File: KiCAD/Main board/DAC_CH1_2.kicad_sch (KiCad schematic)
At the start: 73 parts, among them U1 LM4562, U1 PCM1789, U3 OPA1632DR, U4 OPA1632DR

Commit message: Ad good as finilized the main board schematic
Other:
- note added: "Adress=0"
- note added: "Combine I2C busses of the DACs? Otherwise they can get the same adress."
- note removed: "-Use Panasonic 0805 ERA series for audio path resistors -Use C0G MLCC capacitors for audio path capacitors"
- title: (none) -> AUDIO-DSP_MAIN_BOARD
- moved on the sheet: C1, C10, C11, C15, C16, C19, C2, C3, C4, C6, C7, C8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

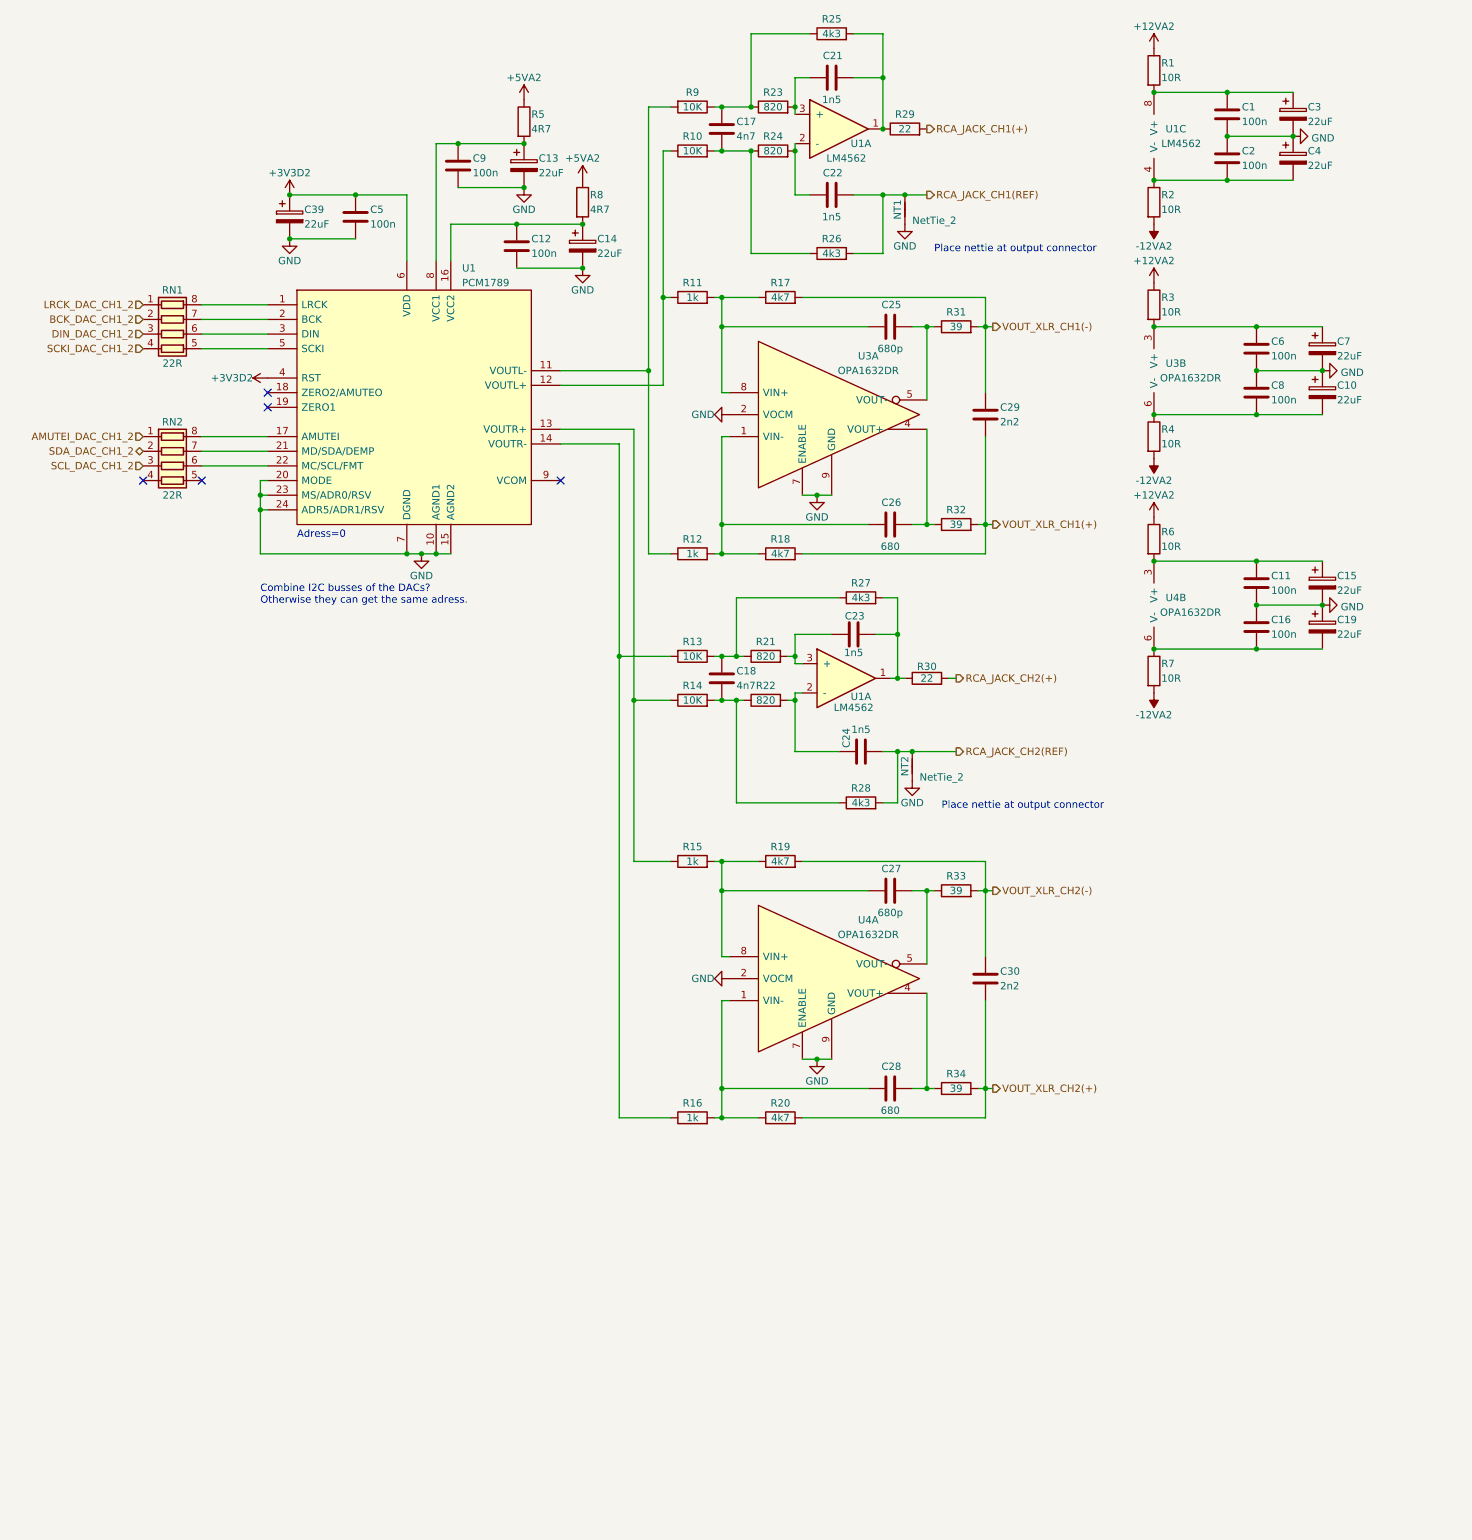
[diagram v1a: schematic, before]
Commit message: Finalizer main board schematic exept passive order links. Schematic ready for review
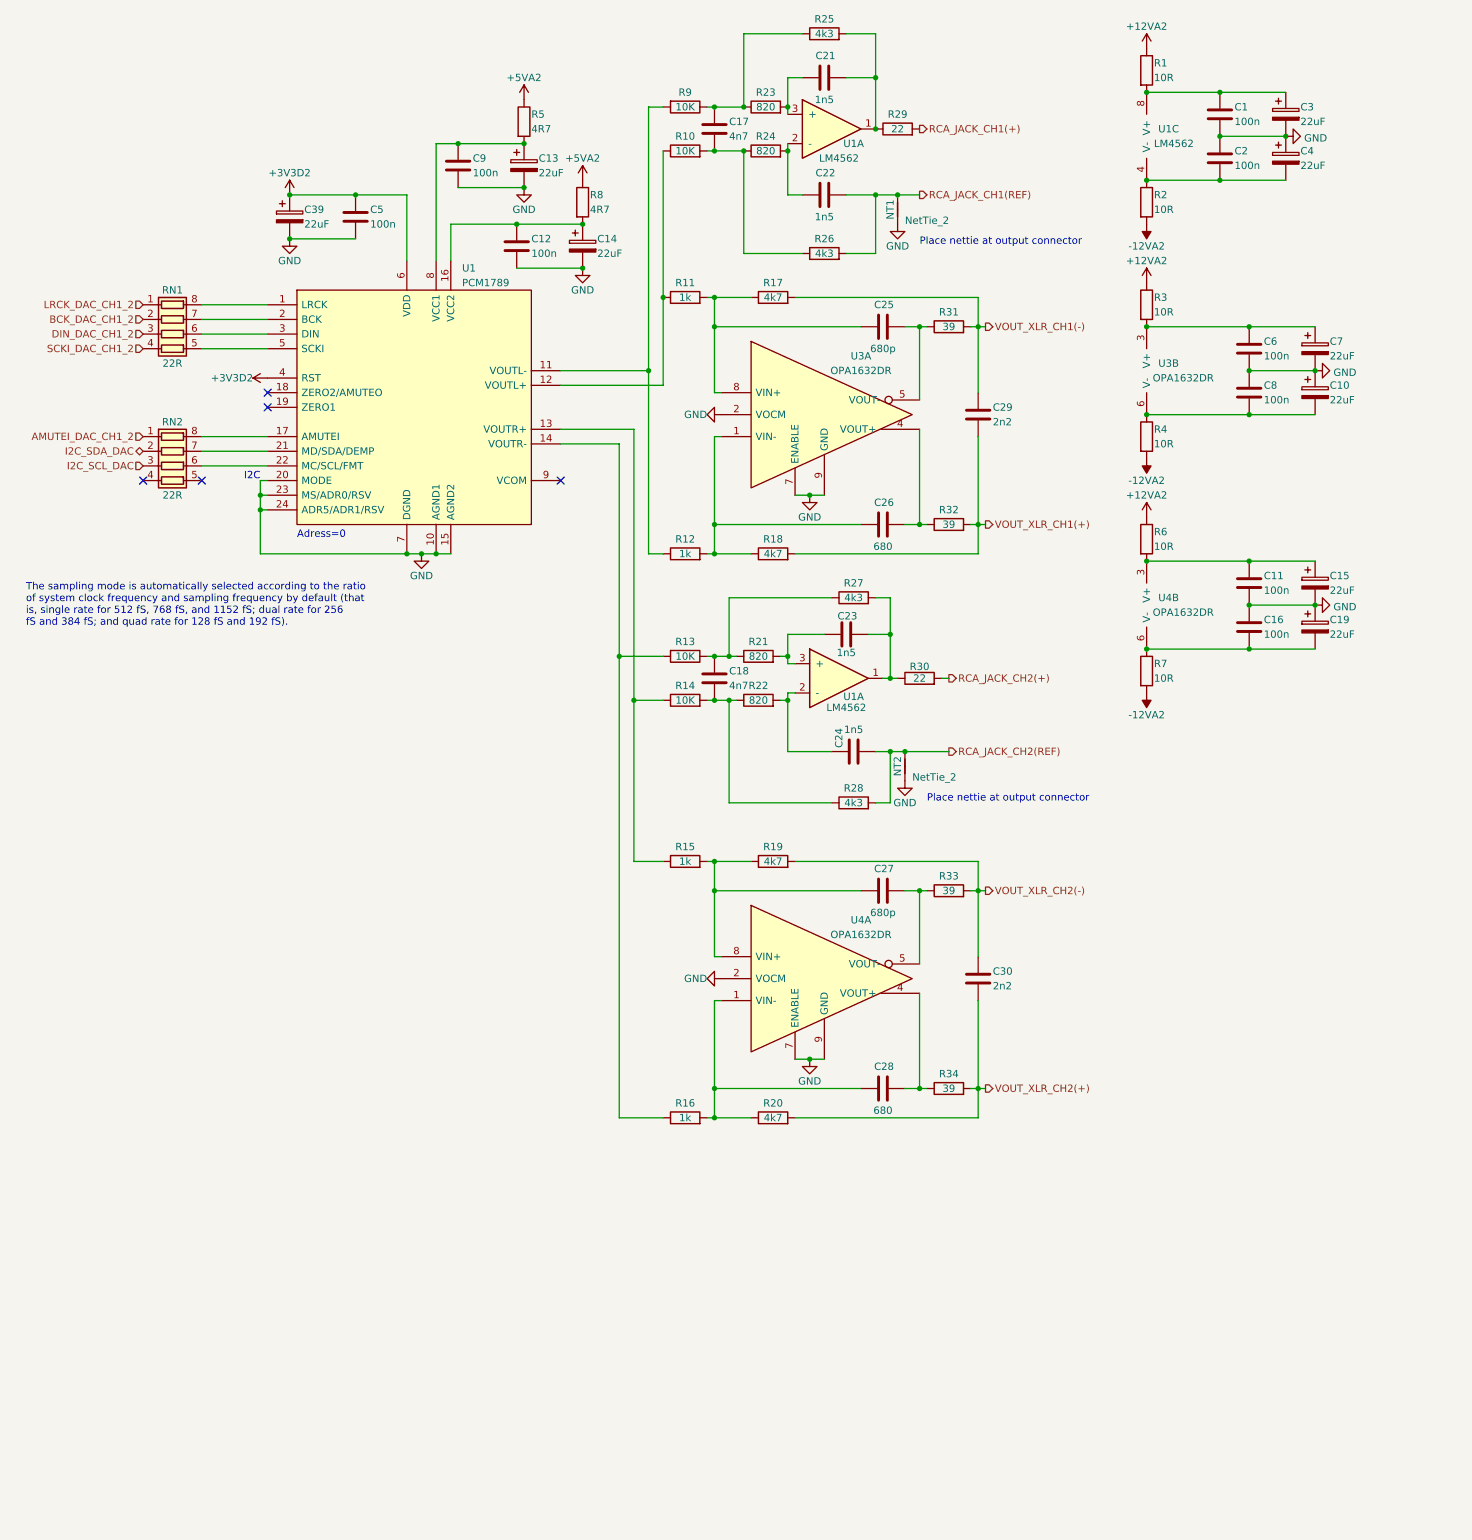
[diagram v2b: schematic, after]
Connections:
- net SCL_DAC_CH1_2 renamed I2C_SCL_DAC
- net SDA_DAC_CH1_2 renamed I2C_SDA_DAC
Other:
- note added: "I2C"
- note added: "The sampling mode is automatically selected according to the ratio of system clock frequency and sampling frequency by default (that is, single rate for 512 fS, 768 fS, and 1152 fS; dual rate for 256 fS and 384 fS; and quad rate for 128 fS and 192 fS)."
- note removed: "Combine I2C busses of the DACs? Otherwise they can get the same adress."
- moved on the sheet: C1, C10, C11, C15, C16, C17, C18, C19, C2, C21, C22, C23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

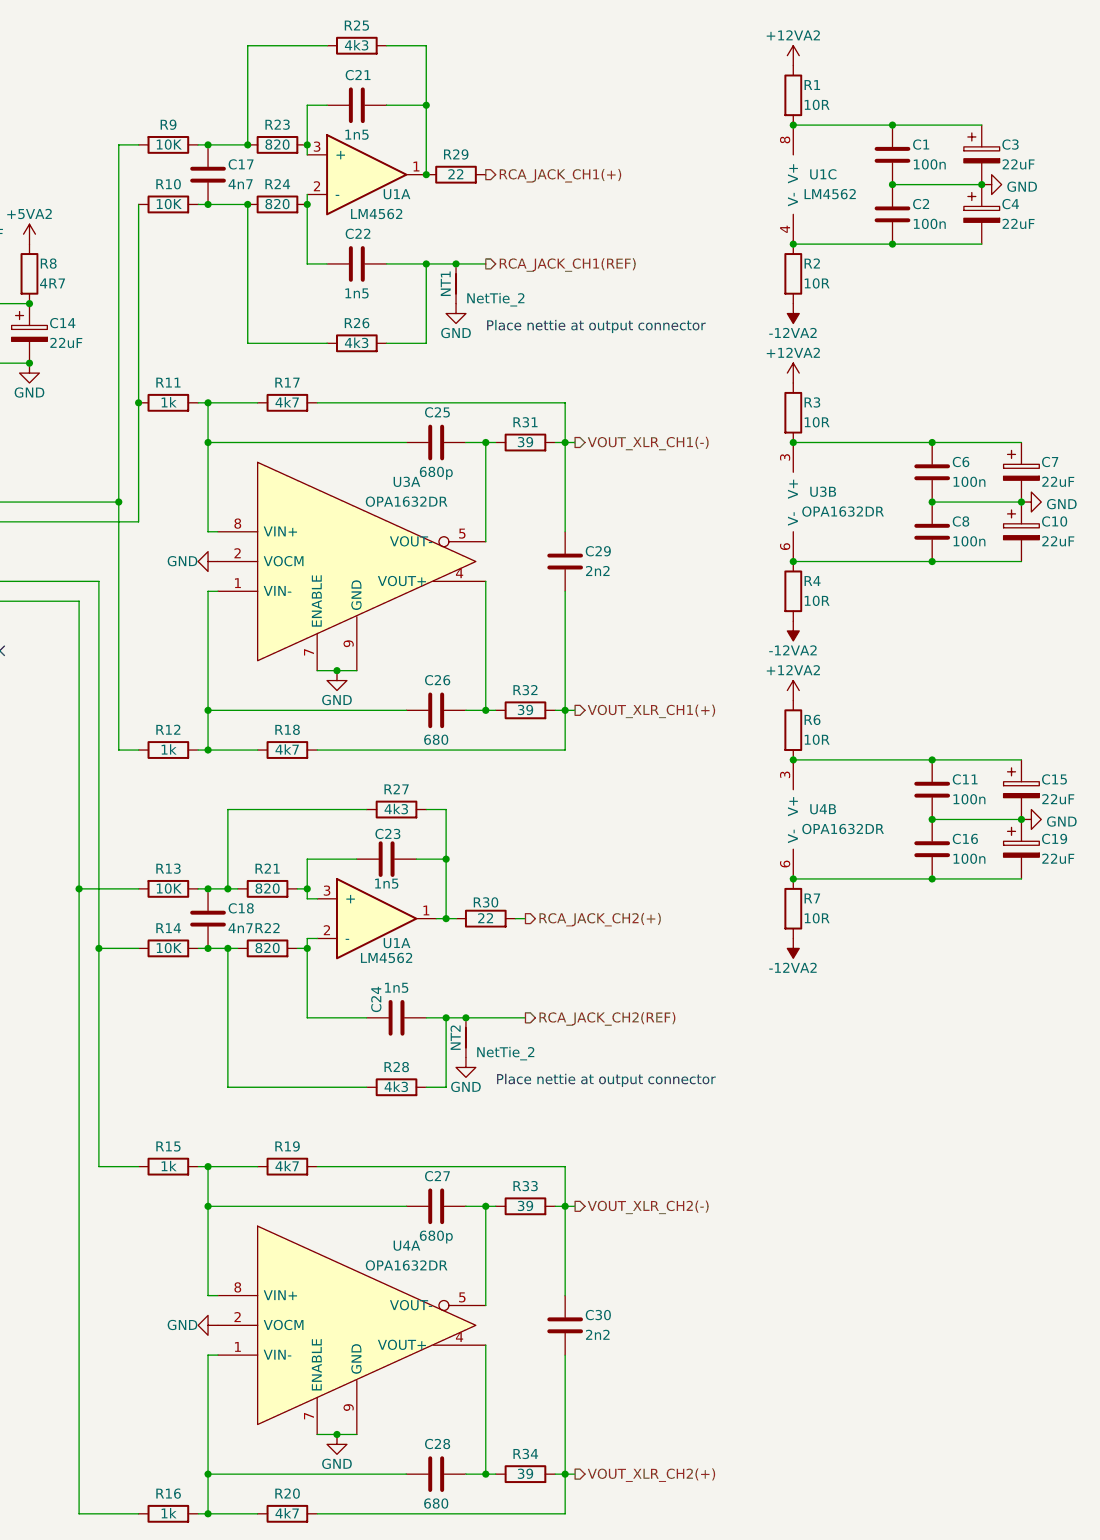
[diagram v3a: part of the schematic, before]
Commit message: Added component links
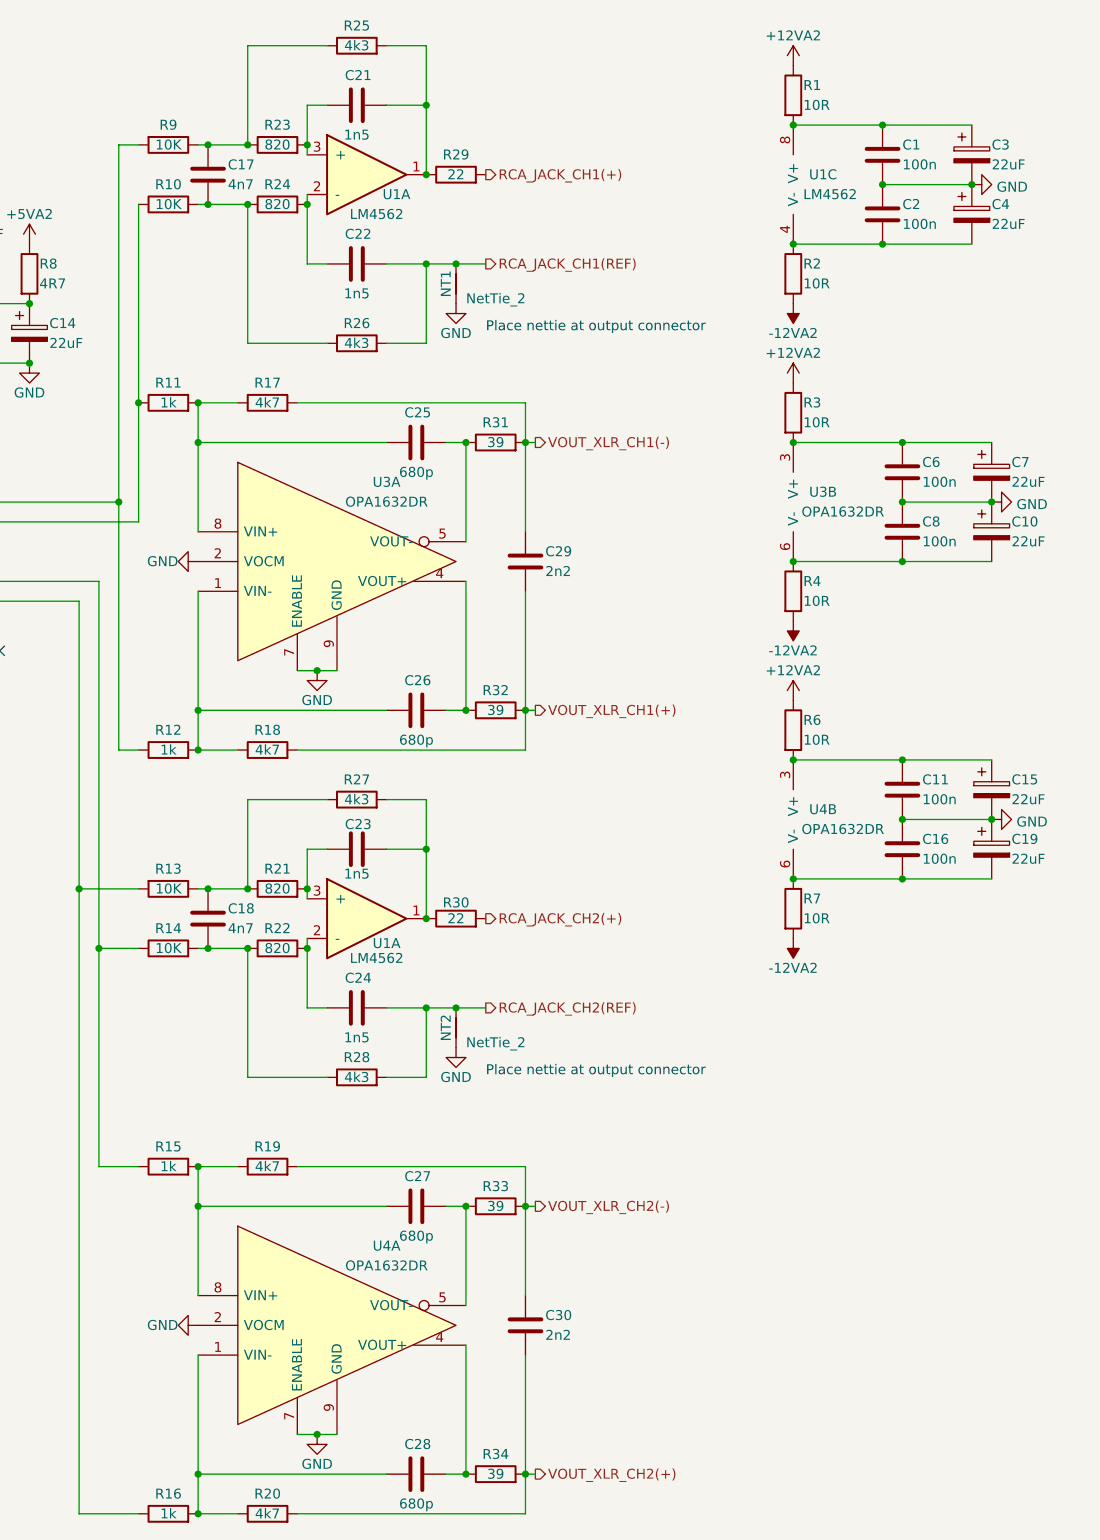
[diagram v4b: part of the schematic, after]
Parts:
- C26, C28: value 680 -> 680p
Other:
- moved on the sheet: C1, C10, C11, C15, C16, C19, C2, C23, C24, C25, C26, C27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

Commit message: Update
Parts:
- NT2: footprint Audio-DSP:NetTie-2_SMD_Pad0.3mm -> NetTie:NetTie-2_SMD_Pad0.5mm
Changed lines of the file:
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@@
       (effects (font (size 1.27 1.27)) (justify right))
     )
-    (property "Footprint" "Audio-DSP:NetTie-2_SMD_Pad0.3mm" (at 163.83 142.24 0)
+    (property "Footprint" "NetTie:NetTie-2_SMD_Pad0.5mm" (at 163.83 142.24 0)
       (effects (font (size 1.27 1.27)) hide)
     )

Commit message: Main board
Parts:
- removed NT1: NetTie_2, Audio-DSP:NetTie-2_SMD_Pad0.3mm, symbol Device:NetTie_2
- removed NT2: NetTie_2, NetTie:NetTie-2_SMD_Pad0.5mm, symbol Device:NetTie_2
- added R215, R216: 0R, Resistor_SMD:R_0402_1005Metric, symbol Device:R
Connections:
- net GND: now also R215.2, R216.2
- net RCA_JACK_CH1(REF): now also R216.1
- net RCA_JACK_CH2(REF): now also R215.1
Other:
- note added: "Place junmper at output connector"
- note removed: "Place nettie at output connector"
